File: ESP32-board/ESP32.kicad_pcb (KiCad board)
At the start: 2 copper layers, 42 parts, among them J1 USB_C_Receptacle_USB2.0, J2 Conn_02x03_Odd_Even, J4 Conn_01x04, J5 Pin_2x5, SW1 USER_SW, SW2 BOOT, SW3 SW_SPST, U1 ESP32-S3-WROOM-1-N16, U2 Si7021-A20, U3 LM1117DT-1.8, U4 USBLC6-2SC6

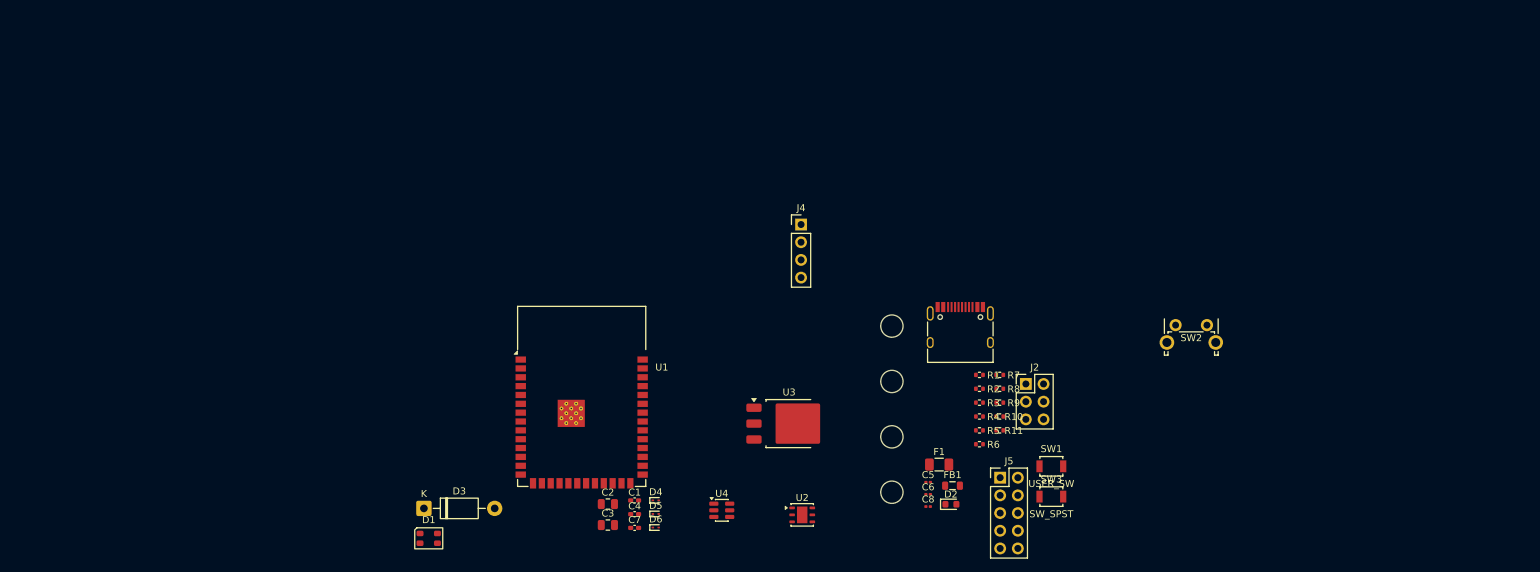
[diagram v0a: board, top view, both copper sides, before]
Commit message: placed esp32 module, holes
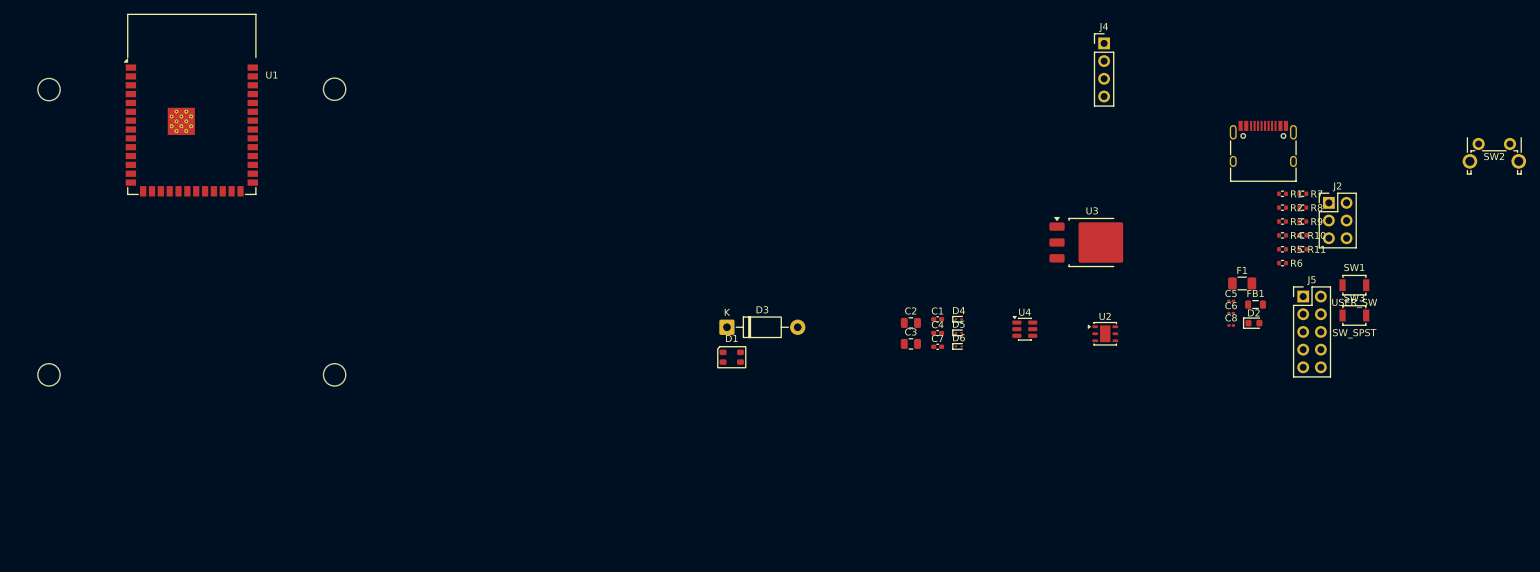
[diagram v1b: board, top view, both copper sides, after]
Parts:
- H1, H2, H3, H4: value MountingHole -> (none)
- moved H1 125.7 mm to (41.5, 44.5)
- moved H4 122.2 mm to (41.5, 85.5)
- moved H2 90.3 mm to (82.5, 44.5)
- moved H3 80.5 mm to (82.5, 85.5)
- moved U1 69.9 mm to (62.0, 46.6)
- moved C1 50.7 mm to (169.1, 77.5)
- moved C4 50.7 mm to (169.1, 79.5)
- moved C5 50.7 mm to (211.2, 74.9)
- moved C6 50.7 mm to (211.2, 76.7)
- moved C7 50.7 mm to (169.1, 81.5)
- moved C8 50.7 mm to (211.2, 78.4)
- moved D2 50.7 mm to (214.5, 78.1)
- moved D3 50.7 mm to (138.8, 78.7)
- moved D4 50.7 mm to (172.1, 77.5)
- moved D5 50.7 mm to (172.1, 79.5)
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
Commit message: layout started
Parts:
- C1, C4, C7: footprint Capacitor_SMD:C_0402_1005Metric_Pad0.74x0.62mm_HandSolder -> Morten_Library:C_0402_1005Metric_Pad0.74x0.62mm_HandSolder
- C2, C3: footprint Capacitor_SMD:C_0805_2012Metric -> Morten_Library:C_0805_2012Metric
- C5, C6, C8: footprint Capacitor_SMD:C_0201_0603Metric -> Morten_Library:C_0603_1608Metric
- D1: footprint LED_SMD:LED_Cree-PLCC4_3.2x2.8mm_CCW -> Morten_Library:LED_Cree-PLCC4_3.2x2.8mm_CCW
- D2: footprint LED_SMD:LED_0603_1608Metric -> Morten_Library:LED_0603_1608Metric
- D3: footprint Diode_THT:D_DO-41_SOD81_P10.16mm_Horizontal -> Morten_Library:D_SOD-123
- F1: footprint Fuse:Fuse_1206_3216Metric -> Morten_Library:Fuse_1206_3216Metric
- H1, H2, H3, H4: value (none) -> MountingHole
- J1: footprint Morten_Library:USB_C_Receptacle_HRO_TYPE-C-31-M-12 -> Connector_USB:USB_C_Receptacle_GCT_USB4105-xx-A_16P_TopMnt_Horizontal
- J4: footprint Connector_PinHeader_2.54mm:PinHeader_1x04_P2.54mm_Vertical -> Connector_JST:JST_SH_SM04B-SRSS-TB_1x04-1MP_P1.00mm_Horizontal
- SW1: renamed from SW3; value SW_SPST -> RESET
- SW2: footprint Morten_Library:SW_Tactile_SPST_Angled_PTS645Vx31-2LFS -> Morten_Library:SW_SPST_B3U-1000P
- SW3: renamed from SW1; footprint Morten_Library:SW_SPST_B3U-1000P -> Morten_Library:SW_Tactile_SPST_Angled_PTS645Vx31-2LFS
- U2: footprint Package_DFN_QFN:DFN-6-1EP_3x3mm_P1mm_EP1.5x2.4mm -> Morten_Library:DFN-6-1EP_3x3mm_P1mm_EP1.5x2.4mm
- U3: footprint Package_TO_SOT_SMD:TO-252-3_TabPin2 -> Package_TO_SOT_SMD:SOT-223
- moved J2 178.2 mm to (43.8, 61.8)
- moved SW2 164.0 mm to (84.3, 75.3)
- moved FB1 158.1 mm to (56.6, 74.4), turned to 180 degrees
- moved J1 157.5 mm to (62.0, 87.7)
- moved F1 155.8 mm to (57.1, 78.6), turned to -90 degrees
- moved R1 153.1 mm to (66.6, 77.8)
- moved R2 153.0 mm to (66.6, 79.3), turned to 180 degrees
- moved J4 152.3 mm to (41.4, 53.1), turned to -90 degrees
- moved R3 152.3 mm to (66.6, 72.6)
- moved R4 152.3 mm to (66.6, 74.6)
- moved R8 151.1 mm to (70.4, 63.9), turned to 90 degrees
- moved R6 148.6 mm to (70.1, 75.1), turned to 90 degrees
- moved J3 148.5 mm to (76.9, 53.8), turned to 90 degrees
- moved R10 148.5 mm to (73.7, 51.1), turned to -90 degrees
- moved SW3 145.5 mm to (84.0, 58.4), turned to -90 degrees
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- renumbered J5 to J2, J2 to J3
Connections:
- U1 pad 13: /USB_D+ -> /USB_D-
- U1 pad 14: /USB_D- -> /USB_D+
- U4 pad 1: /D+ -> /D-
- U4 pad 3: /D- -> /D+
- U4 pad 4: /USB_D- -> /USB_D+
- U4 pad 6: /USB_D+ -> /USB_D-
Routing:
- net /USB_D-: track 0.00 -> 32.3 mm
- net /USB_D+: track 0.00 -> 31.6 mm
- net /D+: track 0.00 -> 4.22 mm
- net /D-: track 0.00 -> 4.22 mm
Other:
- copper layers 2 -> 4

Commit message: continue layout
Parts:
- C3: footprint Morten_Library:C_0805_2012Metric -> Morten_Library:C_0603_1608Metric
- J1: footprint Connector_USB:USB_C_Receptacle_GCT_USB4105-xx-A_16P_TopMnt_Horizontal -> Morten_Library:USB_C_Receptacle_HRO_TYPE-C-31-M-12
- moved R7 35.8 mm to (49.4, 53.3), turned to -90 degrees
- moved C4 31.2 mm to (50.8, 42.1), turned to 90 degrees
- moved R10 25.0 mm to (48.7, 51.0), turned to 0 degrees
- moved R8 24.6 mm to (48.2, 53.3), turned to -90 degrees
- moved C2 6.80 mm to (45.6, 49.6)
- moved R1 3.36 mm to (69.4, 76.0)
- moved R2 3.36 mm to (69.4, 77.5)
- moved C1 2.18 mm to (65.2, 77.8), turned to -90 degrees
- moved C3 1.86 mm to (48.0, 41.9)
- moved FB1 1.68 mm to (56.6, 72.7)
- moved R9 1.68 mm to (77.5, 72.2)
- moved D1 1.68 mm to (73.8, 73.3)
- moved F1 1.68 mm to (57.0, 76.9)
- moved D2 1.68 mm to (80.2, 73.8)
- moved D3 1.68 mm to (56.5, 69.8)
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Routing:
- net /SCL: track 0.00 -> 20.1 mm, vias 0 -> 2
- net /SDA: track 0.00 -> 11.1 mm, vias 0 -> 1
- net +3V3: track 0.00 -> 10.2 mm, vias 0 -> 4
- net GND: track 0.00 -> 5.53 mm, vias 0 -> 4
- net +5V: track 0.00 -> 5.34 mm, vias 0 -> 1
- net /USB_D-: track 32.3 -> 31.6 mm
- net /USB_D+: track 31.6 -> 30.9 mm

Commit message: continue layout
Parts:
- C5: renamed from C2; footprint Morten_Library:C_0805_2012Metric -> Morten_Library:C_0603_1608Metric
- U3: footprint Package_TO_SOT_SMD:SOT-223 -> Package_TO_SOT_SMD:SOT-223-3_TabPin2
- moved C8 44.9 mm to (72.7, 81.3), turned to -90 degrees
- moved C6 43.6 mm to (49.5, 85.5), turned to -90 degrees
- moved D3 41.3 mm to (39.2, 78.3)
- moved C5 36.4 mm to (51.8, 85.5), turned to -90 degrees
- moved D4 34.9 mm to (42.1, 77.0)
- moved R5 27.2 mm to (39.7, 75.7), turned to 180 degrees
- moved C3 26.6 mm to (50.5, 42.1)
- moved C2 26.4 mm to (47.9, 41.9)
- moved C4 16.0 mm to (70.5, 81.2), turned to -90 degrees
- moved D1 13.3 mm to (54.9, 83.1), turned to 90 degrees
- moved FB1 4.60 mm to (54.9, 77.0), turned to -90 degrees
- moved U3 1.46 mm to (49.5, 79.2)
- moved F1 0.76 mm to (57.7, 77.3)
- moved J2 0.75 mm to (44.5, 61.8)
- renumbered C6 to C2, C7 to C3, C5 to C4, C3 to C6, C8 to C7, C4 to C8, D3 to D1, D4 to D2, D2 to D3, D5 to D4, D1 to D5, R10 to R1, R8 to R10, R7 to R11, R9 to R2, R1 to R3, R2 to R4, R3 to R5, R4 to R6, R5 to R7, R11 to R8, R6 to R9, U4 to U1, U1 to U2, U2 to U4
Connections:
- R5 pad 1: +5V -> +3V3
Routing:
- net Net-(U2-GPIO3): track 0.00 -> 16.5 mm, vias 0 -> 2
- net +3V3: track 10.2 -> 20.8 mm, vias 4 -> 5
- net +5V: track 5.34 -> 10.7 mm
- net Net-(F1-Pad2): track 0.00 -> 4.72 mm
- net Net-(D1-A): track 0.00 -> 3.39 mm
- net Net-(F1-Pad1): track 0.00 -> 2.85 mm
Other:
- board text added: "+3.3V"
- board text added: "CLK"
- board text added: "CS"
- board text added: "GND"
- board text added: "IRQ"
- board text added: "MISO"
- board text added: "MOSI"
- board text added: "QWIIC"
- board text added: "RST"

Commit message: continue layout
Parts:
- moved C8 16.6 mm to (68.8, 65.1)
- moved R9 7.60 mm to (77.6, 72.6), turned to 0 degrees
- moved C7 6.80 mm to (77.3, 69.9)
- moved C4 6.33 mm to (76.2, 78.5)
- moved R7 5.42 mm to (77.6, 74.0), turned to 0 degrees
- moved R2 4.91 mm to (78.8, 67.5)
- moved R6 3.75 mm to (70.1, 74.0), turned to 180 degrees
- moved R3 3.43 mm to (69.4, 79.4)
- moved R4 3.43 mm to (69.4, 80.9)
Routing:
- net /SDA: track 11.1 -> 31.0 mm, vias 1 -> 2
- net /SCL: track 20.1 -> 36.7 mm, vias 2 -> 4
- net /CC1: track 0.00 -> 11.3 mm, vias 0 -> 2
- net /CC2: track 0.00 -> 7.66 mm
- net Net-(F1-Pad2): track 4.72 -> 11.0 mm, vias 0 -> 2
- net GND: track 5.97 -> 9.34 mm, vias 4 -> 7
- net +3V3: track 20.8 -> 23.8 mm, vias 5 -> 6
- net Net-(D5-GK): track 0.00 -> 1.99 mm
- net Net-(D5-BK): track 0.00 -> 1.99 mm
- net Net-(D5-RK): track 0.00 -> 1.96 mm
